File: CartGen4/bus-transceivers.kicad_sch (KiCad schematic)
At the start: 10 parts, among them U3 SN74AVC16827DGGR, U4 SN74AVC16827DGGR

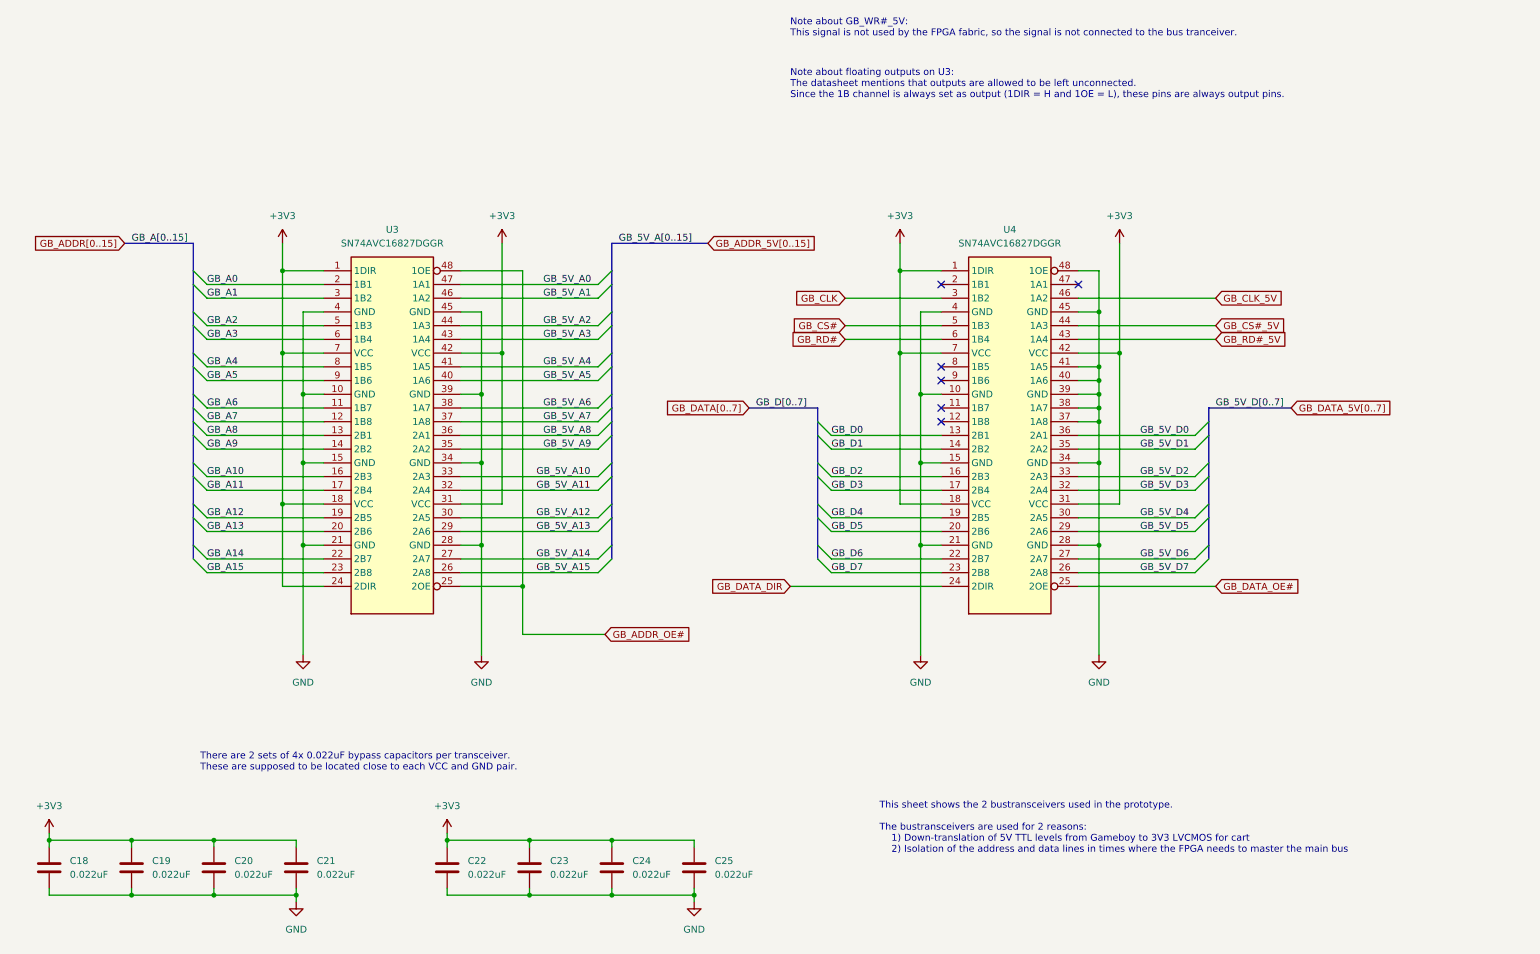
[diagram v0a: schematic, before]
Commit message: Changed bus transceivers
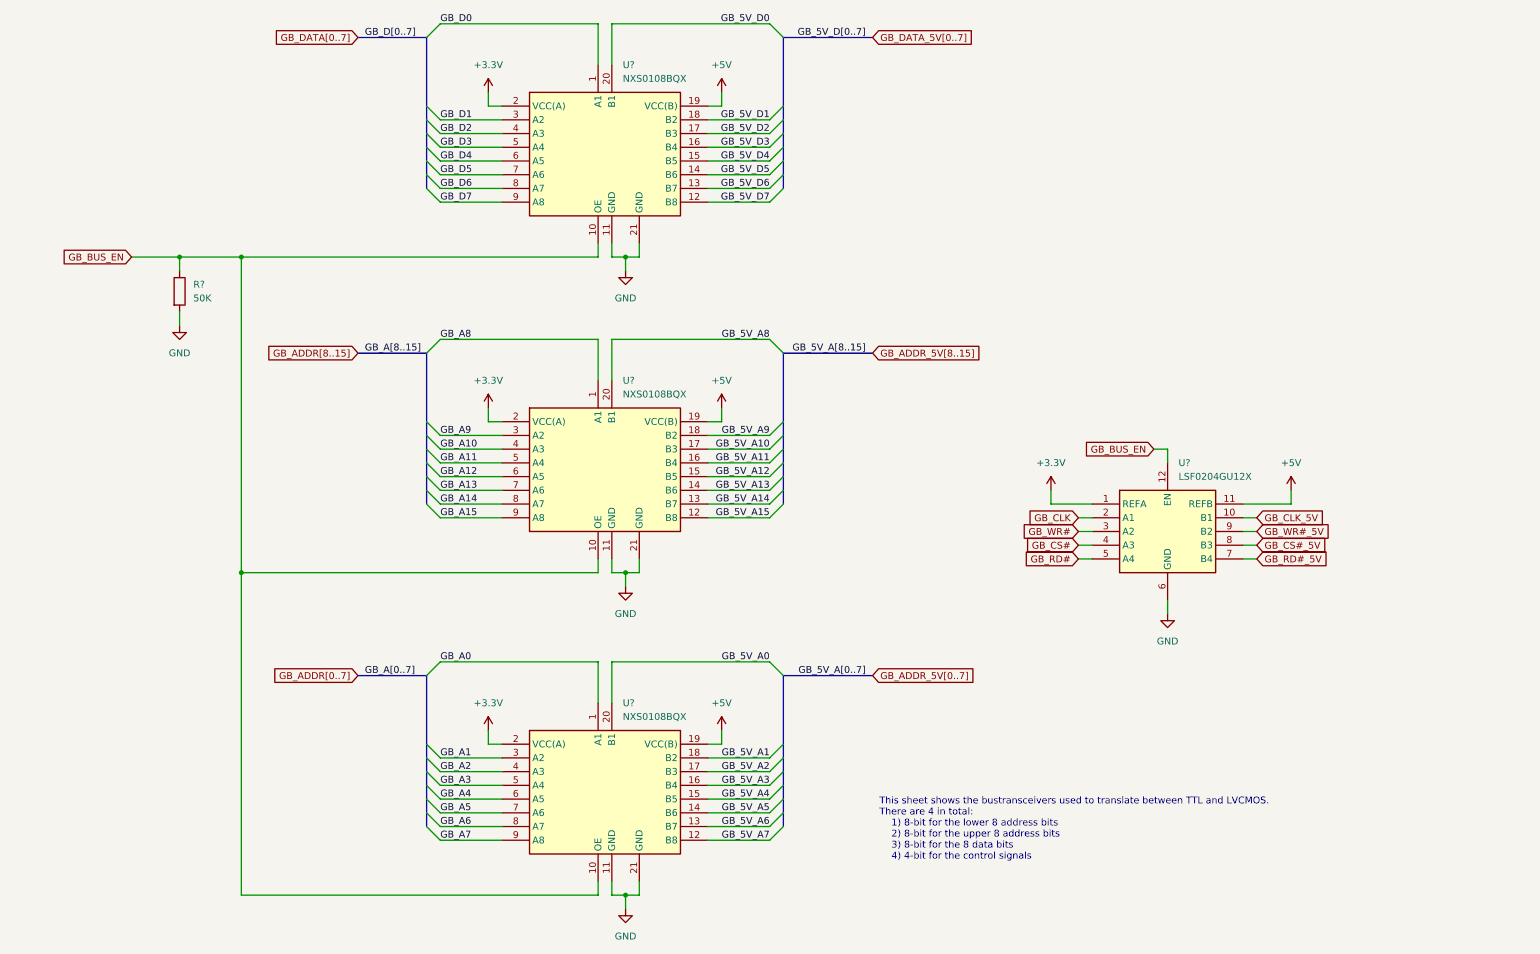
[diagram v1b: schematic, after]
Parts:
- removed C18, C19, C20, C21, C22, C23, C24, C25: 0.022uF, symbol Device:C
- removed U3, U4: SN74AVC16827DGGR, symbol 74xx:SN74AVC16827DGGR
- added R?: 50K, symbol Device:R
- added U? (x3): NXS0108BQX, symbol SamacSys_Parts:NXS0108BQX
- added U?: LSF0204GU12X, symbol SamacSys_Parts:LSF0204GU12X
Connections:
- net +3V3: now also U?.1 (REFA), U?.2 (VCC(A)), U?.2 (VCC(A)), U?.2 (VCC(A))
- net GB_5V_A0: now also U?.20 (B1)
- net GB_5V_A1: now also U?.18 (B2)
- net GB_5V_A10: now also U?.17 (B3)
- net GB_5V_A11: now also U?.16 (B4)
- net GB_5V_A12: now also U?.15 (B5)
- net GB_5V_A13: now also U?.14 (B6)
- net GB_5V_A14: now also U?.13 (B7)
- net GB_5V_A15: now also U?.12 (B8)
- net GB_5V_A2: now also U?.17 (B3)
- net GB_5V_A3: now also U?.16 (B4)
- net GB_5V_A4: now also U?.15 (B5)
- net GB_5V_A5: now also U?.14 (B6)
- net GB_5V_A6: now also U?.13 (B7)
- net GB_5V_A7: now also U?.12 (B8)
- net GB_5V_A8: now also U?.20 (B1)
- net GB_5V_A9: now also U?.18 (B2)
- net GB_5V_D0: now also U?.20 (B1)
- net GB_5V_D1: now also U?.18 (B2)
- net GB_5V_D2: now also U?.17 (B3)
- net GB_5V_D3: now also U?.16 (B4)
- net GB_5V_D4: now also U?.15 (B5)
- net GB_5V_D5: now also U?.14 (B6)
- net GB_5V_D6: now also U?.13 (B7)
- net GB_5V_D7: now also U?.12 (B8)
- net GB_A0: now also U?.1 (A1)
- net GB_A1: now also U?.3 (A2)
- net GB_A10: now also U?.4 (A3)
- net GB_A11: now also U?.5 (A4)
- net GB_A12: now also U?.6 (A5)
- net GB_A13: now also U?.7 (A6)
- net GB_A14: now also U?.8 (A7)
- net GB_A15: now also U?.9 (A8)
- net GB_A2: now also U?.4 (A3)
- net GB_A3: now also U?.5 (A4)
- net GB_A4: now also U?.6 (A5)
- net GB_A5: now also U?.7 (A6)
- net GB_A6: now also U?.8 (A7)
- net GB_A7: now also U?.9 (A8)
- net GB_A8: now also U?.1 (A1)
- net GB_A9: now also U?.3 (A2)
- net GB_CLK: now also U?.2 (A1)
- net GB_CLK_5V: now also U?.10 (B1)
- net GB_CS#: now also U?.4 (A3)
- net GB_CS#_5V: now also U?.8 (B3)
- net GB_D0: now also U?.1 (A1)
- net GB_D1: now also U?.3 (A2)
- net GB_D2: now also U?.4 (A3)
- net GB_D3: now also U?.5 (A4)
- net GB_D4: now also U?.6 (A5)
- net GB_D5: now also U?.7 (A6)
- net GB_D6: now also U?.8 (A7)
- net GB_D7: now also U?.9 (A8)
- net GB_RD#: now also U?.5 (A4)
- net GB_RD#_5V: now also U?.7 (B4)
- net GND: now also R?.2, U?.11 (GND), U?.11 (GND), U?.11 (GND), U?.21 (GND), U?.21 (GND), U?.21 (GND), U?.6 (GND)
- new net +5V: U?.11 (REFB), U?.19 (VCC(B)), U?.19 (VCC(B)), U?.19 (VCC(B))
- new net GB_BUS_EN: R?.1, U?.10 (OE), U?.10 (OE), U?.10 (OE), U?.12 (EN)
- new net GB_WR#: U?.3 (A2)
- new net GB_WR#_5V: U?.9 (B2)
- no-connect marks 6 -> 0
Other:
- note added: "This sheet shows the bustransceivers used to translate between TTL and LVCMOS. There are 4 in total: 1) 8-bit for the lower 8 address bits 2) 8-bit for the upper 8 address bits 3) 8-bit for the 8 data bits 4) 4-bit for the control signals"
- note removed: "Note about GB_WR#_5V: This signal is not used by the FPGA fabric, so the signal is not connected to the bus tranceiver."
- note removed: "Note about floating outputs on U3: The datasheet mentions that outputs are allowed to be left unconnected. Since the 1B channel is always set as output (1DIR = H and 1OE = L), these pins are always output pins."
- note removed: "There are 2 sets of 4x 0.022uF bypass capacitors per transceiver. These are supposed to be located close to each VCC and GND pair."
- note removed: "This sheet shows the 2 bustransceivers used in the prototype. The bustransceivers are used for 2 reasons: 1) Down-translation of 5V TTL levels from Gameboy to 3V3 LVCMOS for cart 2) Isolation of the address and data lines in times where the FPGA needs to master the main bus"

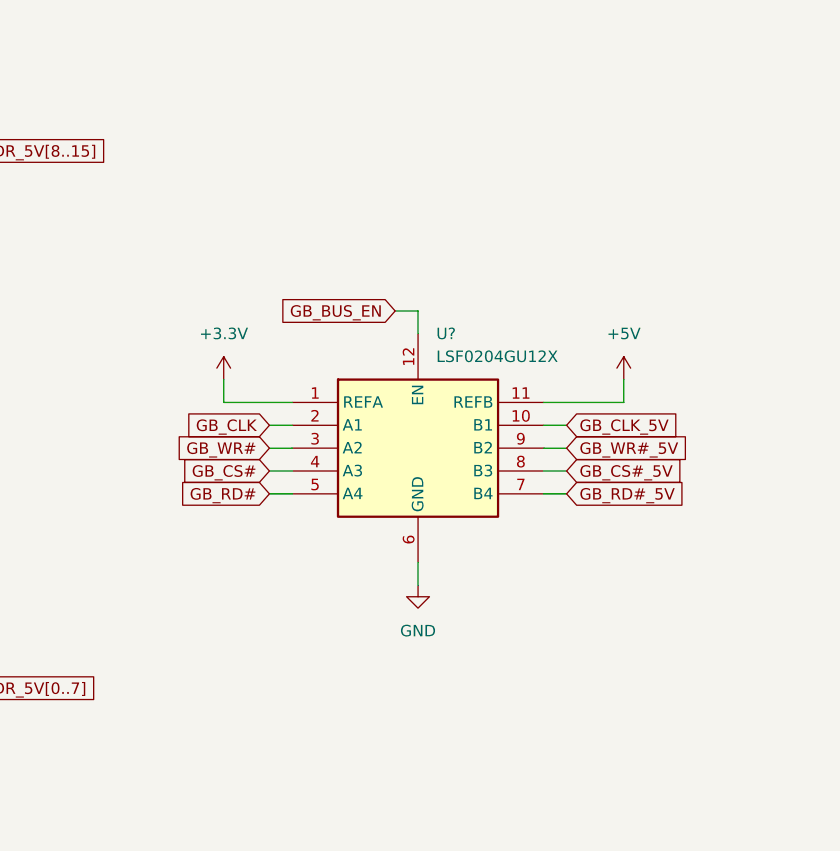
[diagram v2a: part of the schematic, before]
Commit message: Changed control transceiver
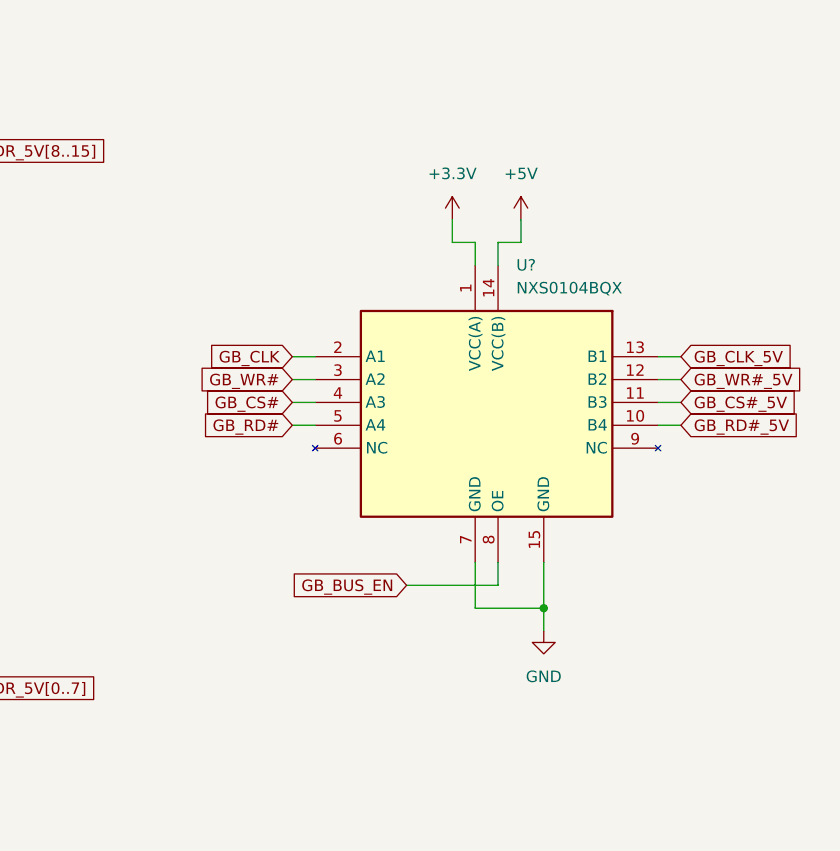
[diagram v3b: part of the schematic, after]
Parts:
- removed U?: LSF0204GU12X, symbol SamacSys_Parts:LSF0204GU12X
- added U?: NXS0104BQX, symbol SamacSys_Parts:NXS0104BQX
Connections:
- net +3V3: now also U?.1 (VCC(A))
- net +5V: now also U?.14 (VCC(B))
- net GB_BUS_EN: now also U?.8 (OE)
- net GB_CLK: now also U?.2 (A1)
- net GB_CLK_5V: now also U?.13 (B1)
- net GB_CS#: now also U?.4 (A3)
- net GB_CS#_5V: now also U?.11 (B3)
- net GB_RD#: now also U?.5 (A4)
- net GB_RD#_5V: now also U?.10 (B4)
- net GB_WR#: now also U?.3 (A2)
- net GB_WR#_5V: now also U?.12 (B2)
- net GND: now also U?.15 (GND), U?.7 (GND)

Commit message: Added copyright
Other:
- company: (none) -> © Elijah Almeida Coimbra
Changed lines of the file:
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@@
   (title_block
     (title "Bus transceivers")
+    (company "© Elijah Almeida Coimbra")
   )
   (junction (at 49.53 67.31) (diameter 0) (color 0 0 0 0)
